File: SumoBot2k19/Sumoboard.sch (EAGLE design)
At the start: 37 parts

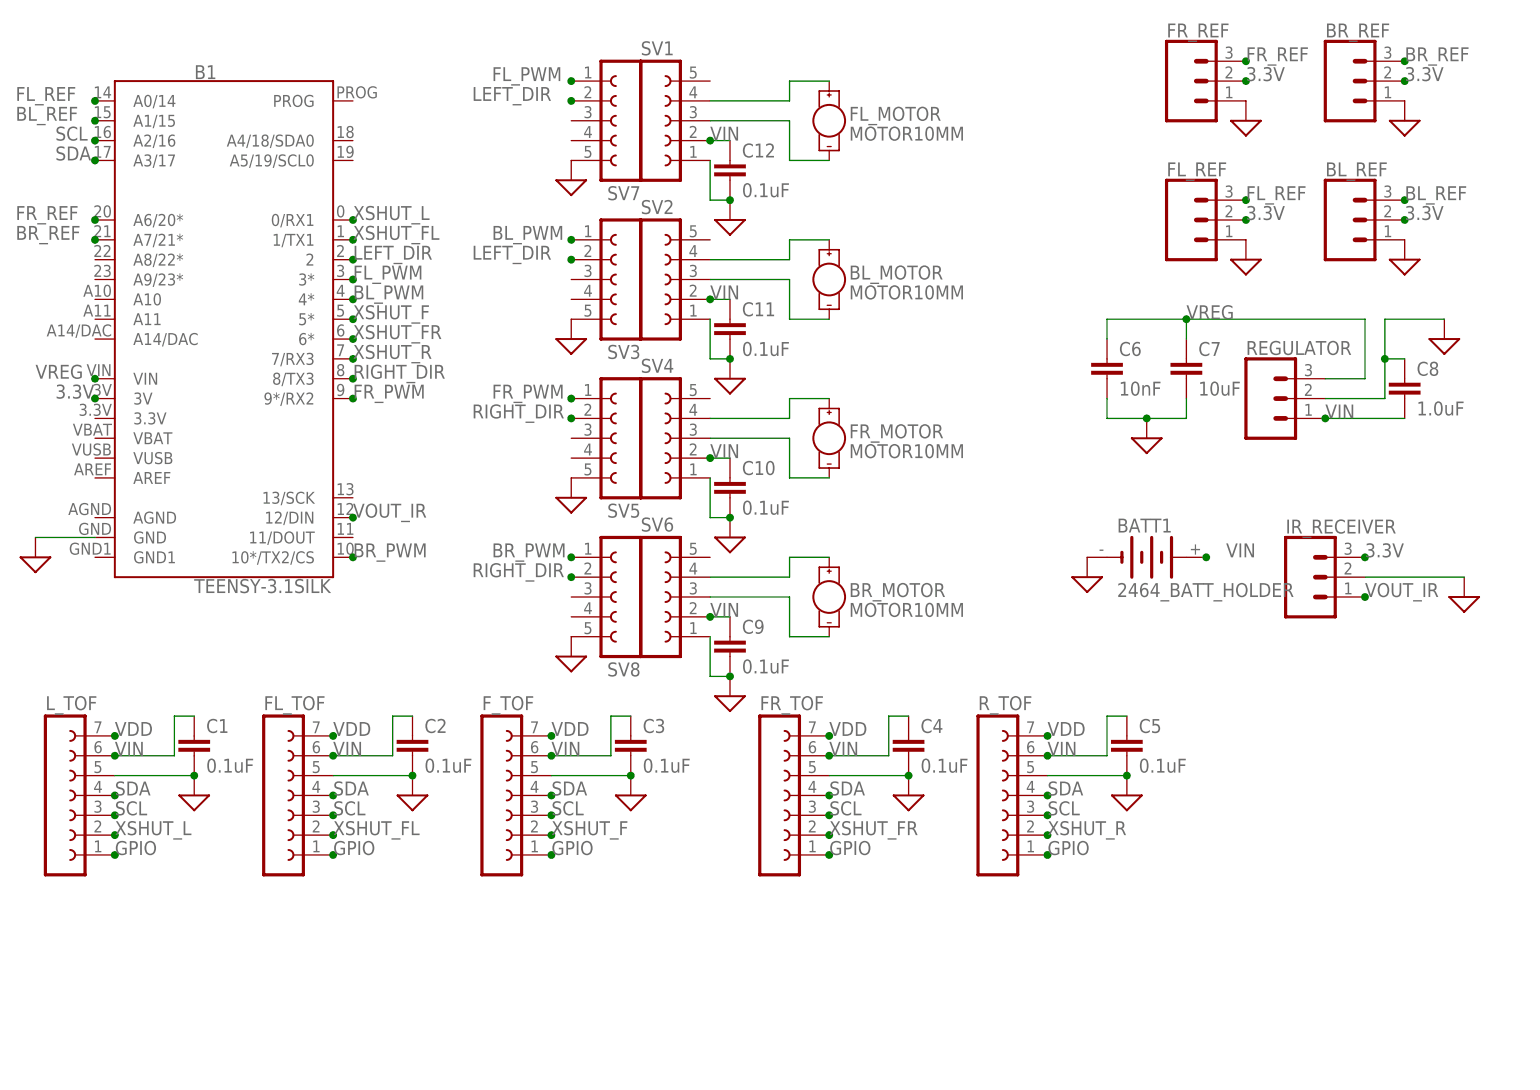
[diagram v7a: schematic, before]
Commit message: changed the REF sensor footprints, changed the TOF input voltage (Vin to 3.3V), connected the FL/BL and FR/BR motor PWMs together
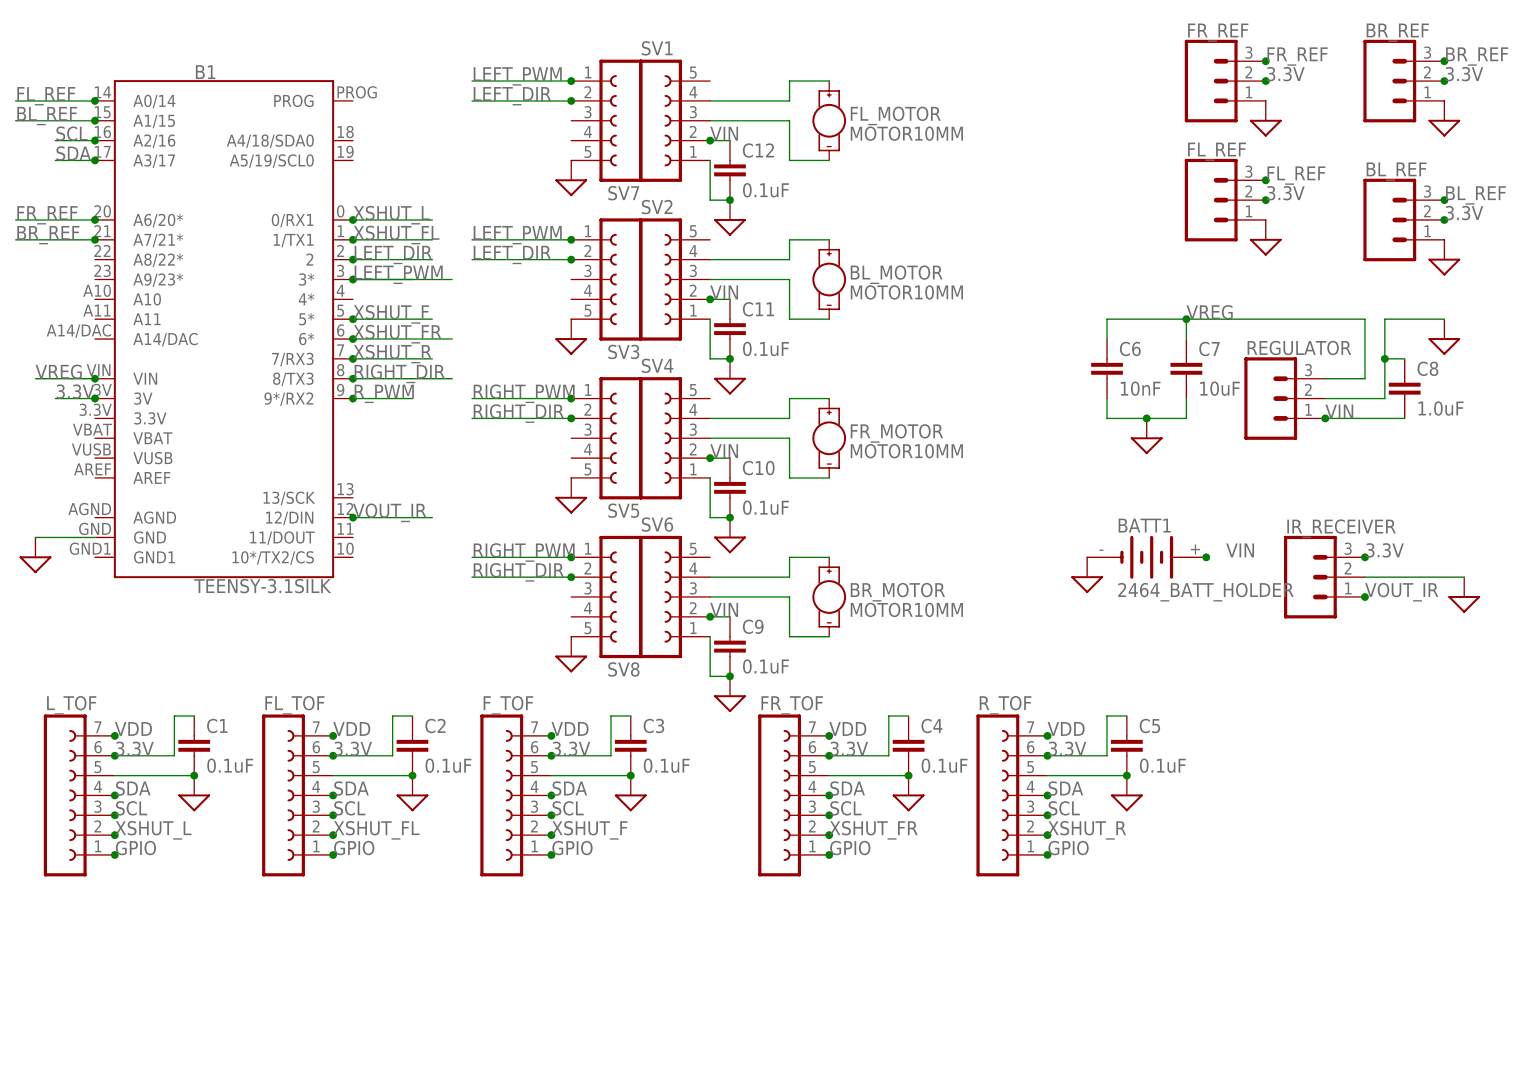
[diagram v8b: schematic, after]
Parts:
- BL_REF, BR_REF, FL_REF, FR_REF: value 3-PIN SMD -> (none); device SparkFun-Connectors:CONN_03JST-SMD -> SparkFun-Connectors:CONN_03
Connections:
- removed net BL_PWM: B1.4*, SV3.1
- removed net BR_PWM: B1.10*/TX2/CS, SV8.1
- removed net FL_PWM: B1.3*, SV7.1
- removed net FR_PWM: B1.9*/RX2, SV5.1
- new net LEFT_PWM: B1.3*, SV3.1, SV7.1
- new net RIGHT_PWM: SV5.1, SV8.1
- new net R_PWM: B1.9*/RX2
- net 3.3V: now also C1.1, C2.1, C3.1, C4.1, C5.1, FL_TOF.6, FR_TOF.6, F_TOF.6, L_TOF.6, R_TOF.6
- net VIN: no longer C1.1, C2.1, C3.1, C4.1, C5.1, FL_TOF.6, FR_TOF.6, F_TOF.6, L_TOF.6, R_TOF.6
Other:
- moved on the sheet: BL_REF, BR_REF, FL_REF, FR_REF
